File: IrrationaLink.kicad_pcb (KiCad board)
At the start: 2 copper layers, 50 x 24 mm, 27 parts, among them J1 USB_C_Receptacle_USB2.0, U1 ESP32-C3, U2 LM2937xMP

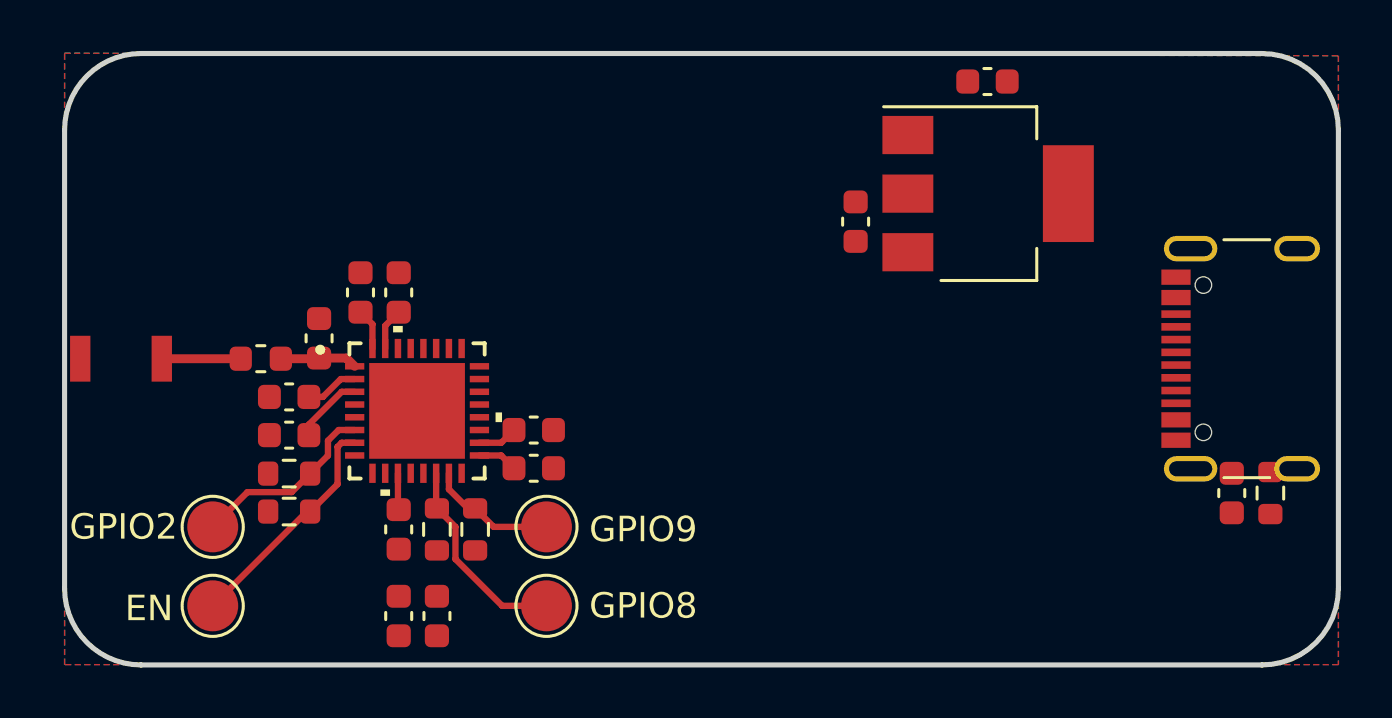
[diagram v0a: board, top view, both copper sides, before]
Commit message: Add gitignore; Route USB lines
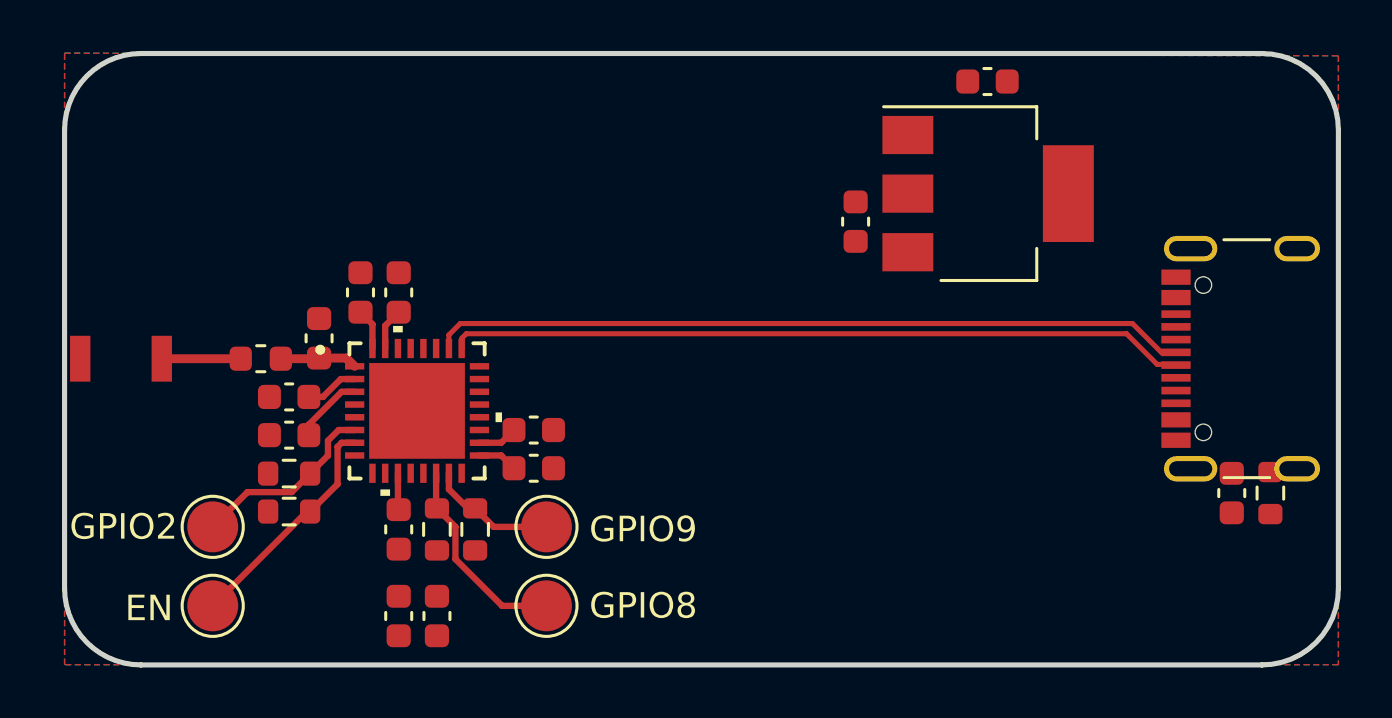
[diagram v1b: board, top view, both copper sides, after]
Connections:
- J1 pad A6: /D- -> /USB_D-
- J1 pad A7: /D+ -> /USB_D+
- J1 pad B6: /D- -> /USB_D-
- J1 pad B7: /D+ -> /USB_D+
- U1 pad 25: unconnected-(U1-GPIO18-Pad25) -> /USB_D-
- U1 pad 26: unconnected-(U1-GPIO19-Pad26) -> /USB_D+
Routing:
- net /USB_D+: track 0.00 -> 29.7 mm
- net /USB_D-: track 0.00 -> 29.0 mm

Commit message: Design first version of board (Crystal not routed yet)
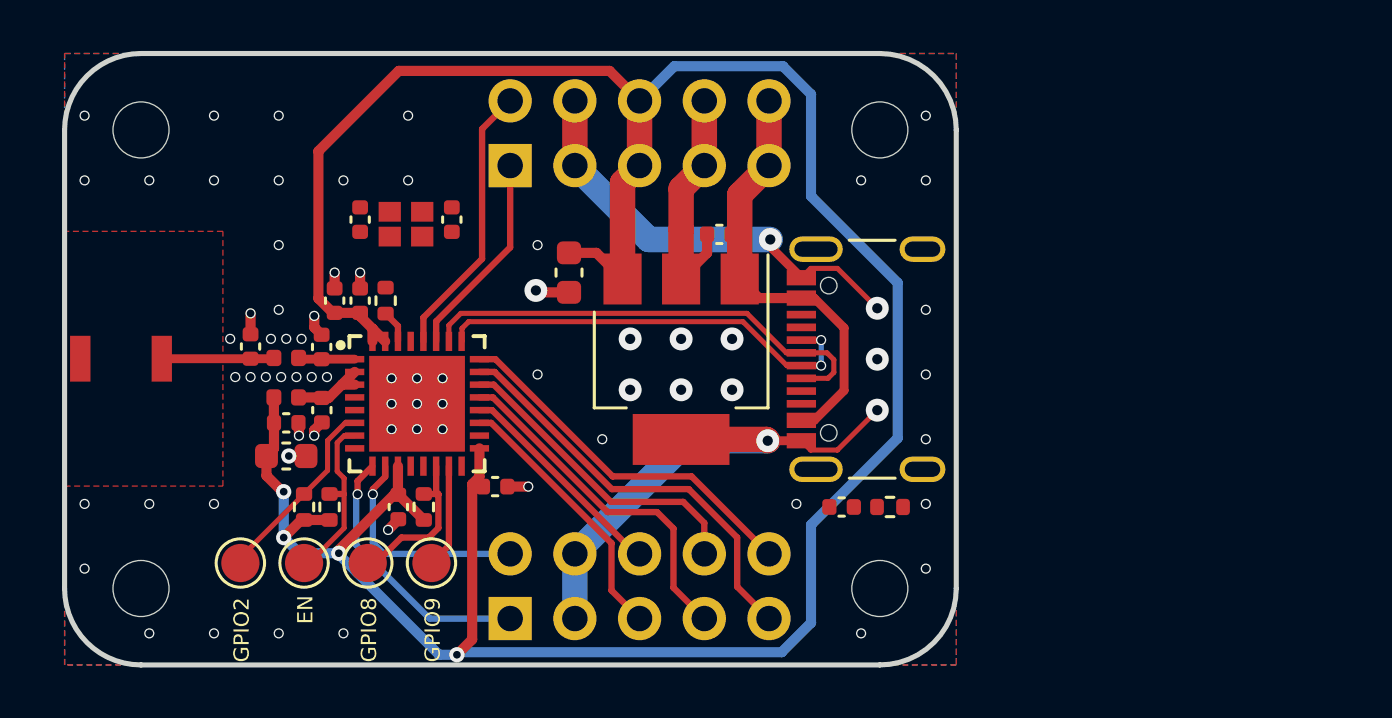
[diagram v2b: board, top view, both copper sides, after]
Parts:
- removed C10, C7: 100n, Capacitor_SMD:C_0603_1608Metric
- removed C8: 1u, Capacitor_SMD:C_0603_1608Metric
- removed C9: 4u7, Capacitor_SMD:C_0603_1608Metric
- removed R5: 10k, Resistor_SMD:R_0603_1608Metric
- added C14: C, Capacitor_SMD:C_0402_1005Metric, F.Cu at (126.3, 81.5)
- added C15: 100n, Capacitor_SMD:C_0402_1005Metric, F.Cu at (129.1, 84.0)
- added C16: 100n, Capacitor_SMD:C_0402_1005Metric, F.Cu at (127.7, 84.5)
- added C17: 100n, Capacitor_SMD:C_0402_1005Metric, F.Cu at (132.1, 87.8)
- added C18: 10u, Capacitor_SMD:C_0603_1608Metric, F.Cu at (127.7, 85.8)
- added H1: MountingHole, MountingHole:MountingHole_2.2mm_M2, F.Cu at (151.0, 91.0)
- added H2: MountingHole, MountingHole:MountingHole_2.2mm_M2, F.Cu at (151.0, 73.0)
- added H3: MountingHole, MountingHole:MountingHole_2.2mm_M2, F.Cu at (122.0, 73.0)
- added H4: MountingHole, MountingHole:MountingHole_2.2mm_M2, F.Cu at (122.0, 91.0)
- added J2: Conn_02x05_Odd_Even, Connector_PinHeader_2.54mm:PinHeader_2x05_P2.54mm_Vertical, F.Cu at (136.5, 92.2)
- added J3: Conn_02x05_Odd_Even, Connector_PinHeader_2.54mm:PinHeader_2x05_P2.54mm_Vertical, F.Cu at (136.5, 74.4)
- added L2: 2n, Inductor_SMD:L_0402_1005Metric, F.Cu at (127.7, 83.5)
- added R6: R, Resistor_SMD:R_0402_1005Metric, F.Cu at (131.6, 79.7)
- added Y1: ABM11W-32.0000MHZ-7-D1X-T3, encyclopedia_galactica:ABM11W-30.0000MHZ-7-D1X-T3, F.Cu at (132.4, 76.7)
- C1, C11, C2: footprint Capacitor_SMD:C_0603_1608Metric -> Capacitor_SMD:C_0402_1005Metric
- C12: value 1u -> 100n; footprint Capacitor_SMD:C_0603_1608Metric -> Capacitor_SMD:C_0402_1005Metric
- C13: value 1u -> 10u
- C3: value 100n -> 10n; footprint Capacitor_SMD:C_0603_1608Metric -> Capacitor_SMD:C_0402_1005Metric
- C4: value 100n -> 1u; footprint Capacitor_SMD:C_0603_1608Metric -> Capacitor_SMD:C_0402_1005Metric
- C5, C6: value 100n -> 12pF; footprint Capacitor_SMD:C_0603_1608Metric -> Capacitor_SMD:C_0402_1005Metric
- L1: footprint Inductor_SMD:L_0603_1608Metric -> Inductor_SMD:L_0402_1005Metric
- R1, R2, R3, R4: footprint Resistor_SMD:R_0603_1608Metric -> Resistor_SMD:R_0402_1005Metric
- TP1, TP2, TP3, TP4: footprint TestPoint:TestPoint_Pad_D2.0mm -> TestPoint:TestPoint_Pad_D1.5mm
- moved C11 15.3 mm to (149.5, 87.8), turned to 0 degrees
- moved R1 14.9 mm to (151.4, 87.8), turned to 180 degrees
- moved J1 14.7 mm to (151.6, 82.0)
- moved U2 13.7 mm to (143.2, 82.0), turned to -90 degrees
- moved C12 12.1 mm to (144.7, 77.1), turned to 180 degrees
- moved C13 11.4 mm to (138.8, 78.6), turned to -90 degrees
- moved C3 10.2 mm to (129.6, 79.7), turned to 90 degrees
- moved C4 9.11 mm to (130.6, 79.7), turned to 90 degrees
- moved C2 8.33 mm to (135.9, 87.0), turned to 0 degrees
- moved TP3 7.21 mm to (130.9, 90.0)
- moved TP2 4.73 mm to (133.4, 90.0)
- moved TP1 3.96 mm to (128.4, 90.0)
- moved C6 3.54 mm to (134.2, 76.5), turned to -90 degrees
- moved C5 2.86 mm to (130.6, 76.5)
- moved TP4 1.79 mm to (125.9, 90.0)
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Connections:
- C5 pad 1: +3V3 -> /XTAL_P
- C6 pad 1: +3V3 -> /XTAL_N
- U1 pad 10: unconnected-(U1-MTDI-Pad10) -> /ADC2_CH0
- U1 pad 18: +3V3 -> unconnected-(U1-VDD_SPI-Pad18)
- U1 pad 19: unconnected-(U1-SPIHD-Pad19) -> /GPIO12
- U1 pad 2: +3V3 -> /VDD3P3
- U1 pad 20: unconnected-(U1-SPIWP-Pad20) -> /GPIO13
- U1 pad 21: unconnected-(U1-SPICS0-Pad21) -> /GPIO14
- U1 pad 22: unconnected-(U1-SPICLK-Pad22) -> /GPIO15
- U1 pad 23: unconnected-(U1-SPID-Pad23) -> /GPIO16
- U1 pad 24: unconnected-(U1-SPIQ-Pad24) -> /GPIO17
- U1 pad 27: unconnected-(U1-U0RXD-Pad27) -> /U0RXD
- U1 pad 28: unconnected-(U1-U0TXD-Pad28) -> /U0TXD
- U1 pad 29: unconnected-(U1-XTAL_N-Pad29) -> /XTAL_N
- U1 pad 3: +3V3 -> /VDD3P3
- U1 pad 30: unconnected-(U1-XTAL_P-Pad30) -> /XTAL_P_RES
- U1 pad 9: unconnected-(U1-MTMS-Pad9) -> /ADC1_CH4
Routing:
- net +3V3: track 12.7 -> 110.7 mm, vias 0 -> 4
- net GND: track 0.00 -> 54.7 mm, vias 0 -> 74
- net VBUS: track 0.00 -> 17.0 mm
- net /GPIO16: track 0.00 -> 16.5 mm
- net /GPIO17: track 0.00 -> 14.5 mm
- net /GPIO14: track 0.00 -> 13.8 mm
- net /GPIO15: track 0.00 -> 12.3 mm
- net /USB_D-: track 29.0 -> 17.2 mm, vias 0 -> 2
- net /USB_D+: track 29.7 -> 18.6 mm
- net /U0TXD: track 0.00 -> 10.9 mm
- net /ADC1_CH4: track 0.00 -> 10.6 mm, vias 0 -> 1
- net /GPIO12: track 0.00 -> 10.6 mm
- net /ADC2_CH0: track 0.00 -> 8.78 mm, vias 0 -> 1
- net /GPIO13: track 0.00 -> 8.62 mm
- net /U0RXD: track 0.00 -> 8.10 mm
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- added copper zone on F.Cu, net GND
- removed copper zone on F.Cu, net unconnected-(U1-MTDO-Pad13)
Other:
- board size 50 x 24 mm -> 35 x 24 mm
- board text added: "+3V3"
- board text added: "12"
- board text added: "13"
- board text added: "14"
- board text added: "15"
- board text added: "16"
- board text added: "17"
- board text added: "ADC1_CH4"
- board text added: "ADC2_CH0"
- board text added: "EN"
- board text added: "GND"
- board text added: "GPIO2"
- board text added: "GPIO8"
- board text added: "GPIO9"
- board text added: "GPIOx"
- board text added: "IrrationaLink v1.0"
- board text added: "U0RXD"
- board text added: "U0TXD"
- board text added: "VBUS"

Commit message: Remove board name; Minor other changes
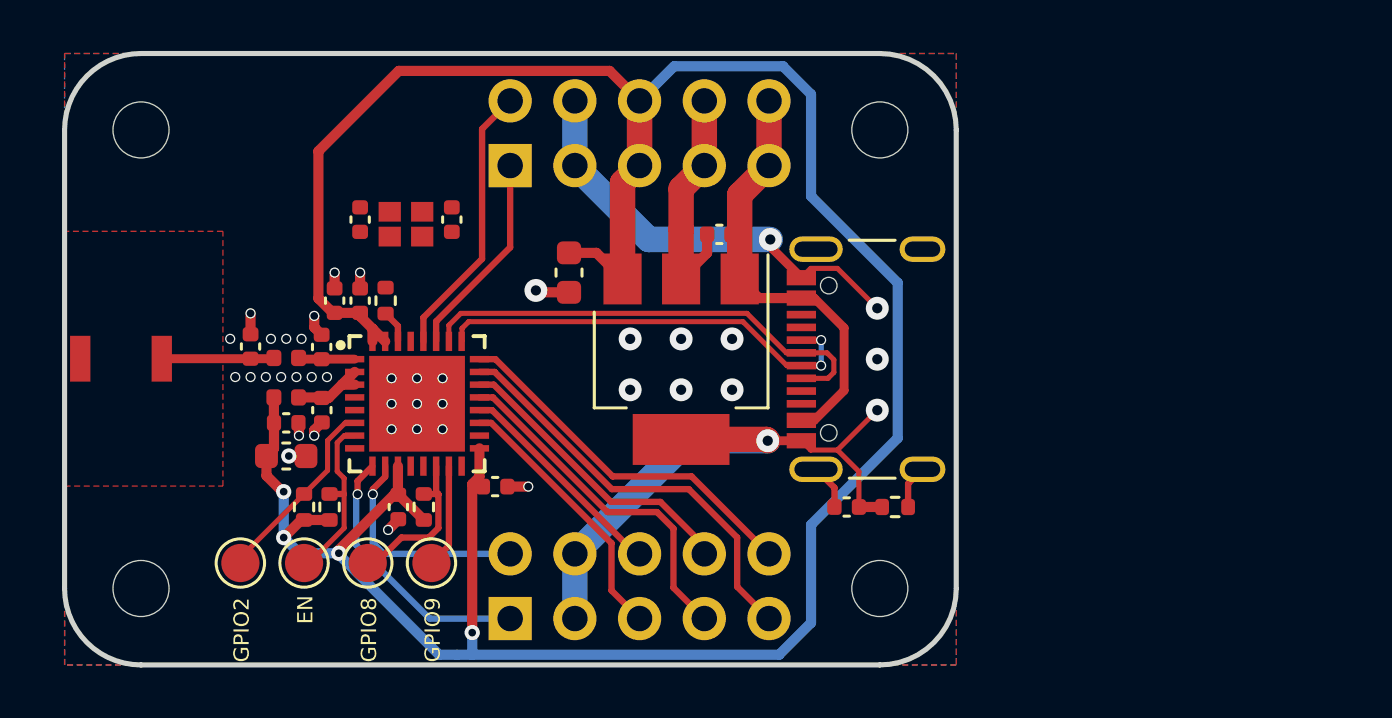
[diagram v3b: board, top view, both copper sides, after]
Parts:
- moved C11 0.20 mm to (149.7, 87.8)
- moved R1 0.20 mm to (151.6, 87.8)
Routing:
- net GND: track 54.7 -> 58.2 mm, vias 74 -> 41
- net /SHIELD: track 0.00 -> 3.49 mm
- net /GPIO15: track 12.3 -> 11.8 mm
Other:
- board text removed: "IrrationaLink v1.0"

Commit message: Add button; Move power lines
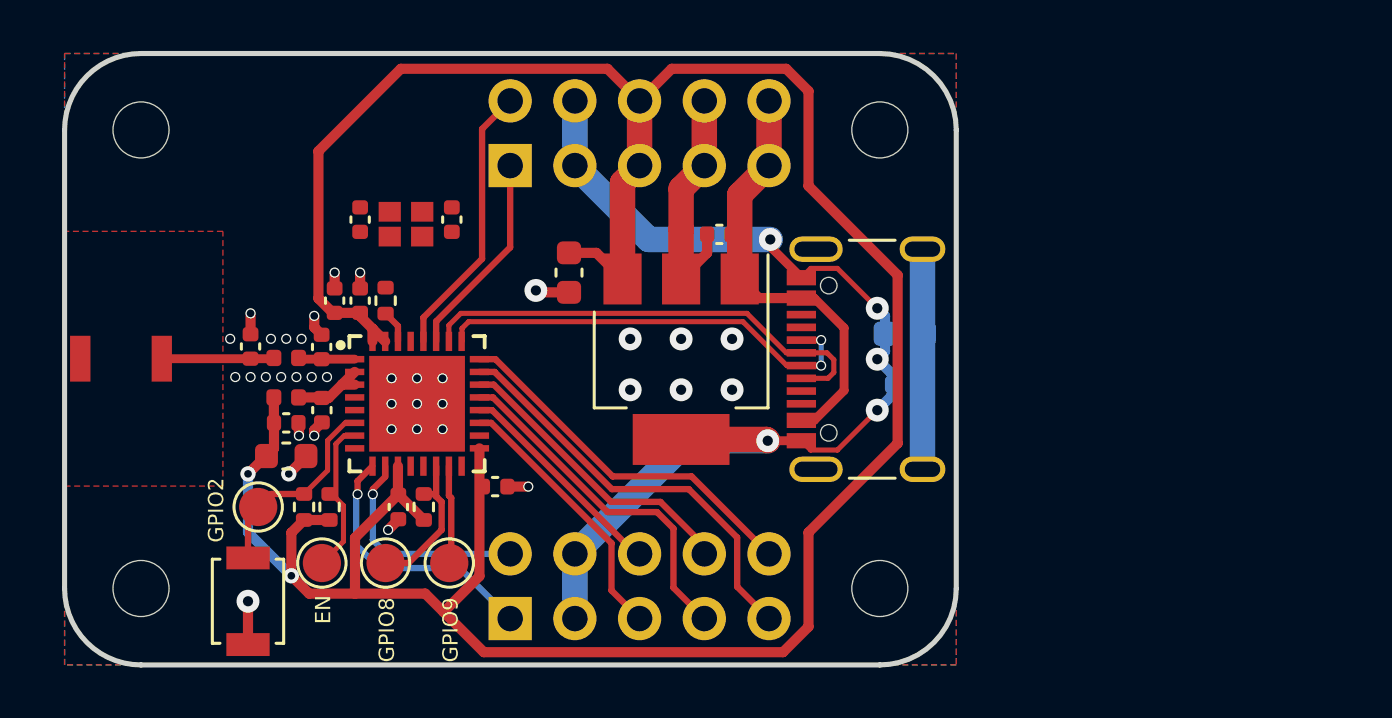
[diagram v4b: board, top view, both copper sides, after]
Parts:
- added SW1: SW_Push, Button_Switch_SMD:SW_SPST_B3U-1000P, F.Cu at (126.2, 91.5)
- C11: footprint Capacitor_SMD:C_0402_1005Metric -> Capacitor_SMD:C_0603_1608Metric; moved to B.Cu
- R1: moved to B.Cu
- moved C11 7.17 mm to (152.0, 81.0), turned to 180 degrees
- moved R1 4.82 mm to (152.0, 83.0)
- moved TP4 2.31 mm to (126.6, 87.8)
- moved TP1 0.70 mm to (129.1, 90.0)
- moved TP2 0.70 mm to (134.1, 90.0)
- moved TP3 0.70 mm to (131.6, 90.0)
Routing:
- net /SHIELD: track 3.49 -> 8.64 mm
- net GND: track 58.2 -> 61.4 mm, vias 41 -> 42
- net +3V3: track 110.5 -> 113.0 mm, vias 4 -> 2
- net /EN: track 6.98 -> 6.02 mm
- net /GPIO8: track 6.38 -> 5.85 mm

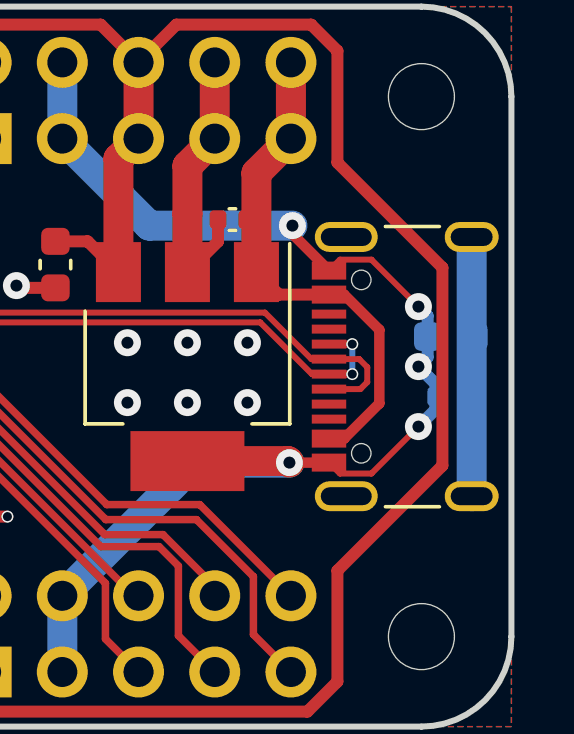
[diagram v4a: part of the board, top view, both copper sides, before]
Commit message: Move shield resistor and cap to front
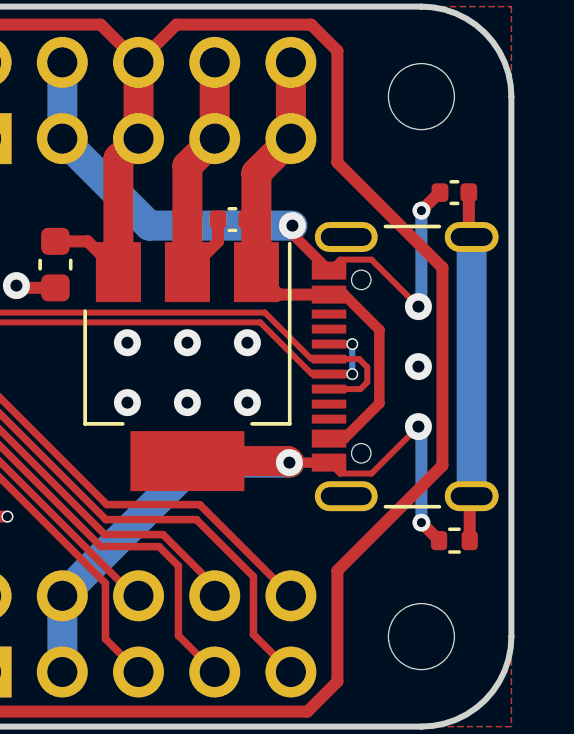
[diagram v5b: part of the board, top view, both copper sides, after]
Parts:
- C11: footprint Capacitor_SMD:C_0603_1608Metric -> Capacitor_SMD:C_0402_1005Metric; moved to F.Cu
- R1: moved to F.Cu
- moved C11 4.80 mm to (152.1, 76.2)
- moved R1 4.80 mm to (152.1, 87.8)
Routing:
- net GND: track 61.4 -> 64.9 mm, vias 42 -> 44
- net /SHIELD: track 8.64 -> 11.7 mm
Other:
- board text added: "HyperLink v1.0"

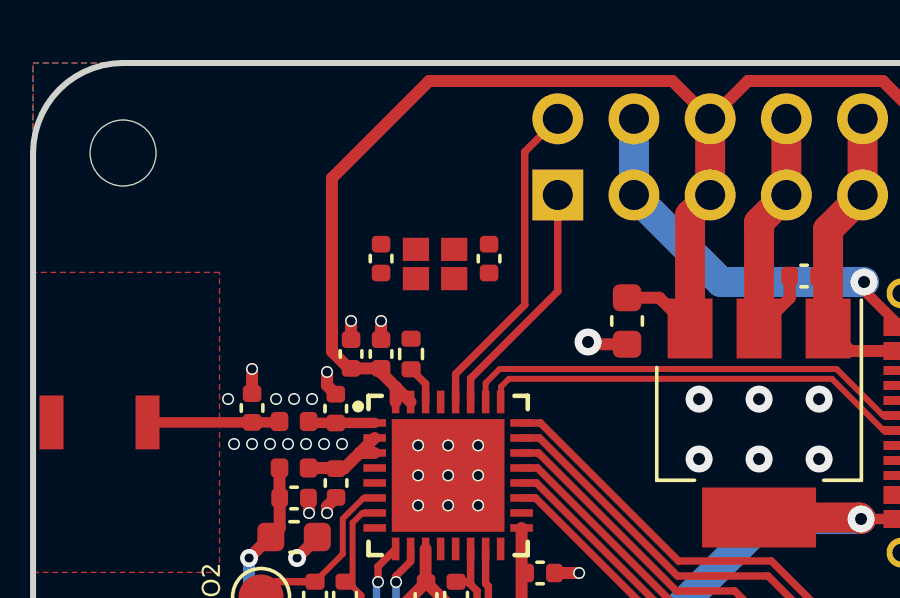
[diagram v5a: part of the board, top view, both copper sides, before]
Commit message: Connect Crystal; Add 500R resistor to U0TXD
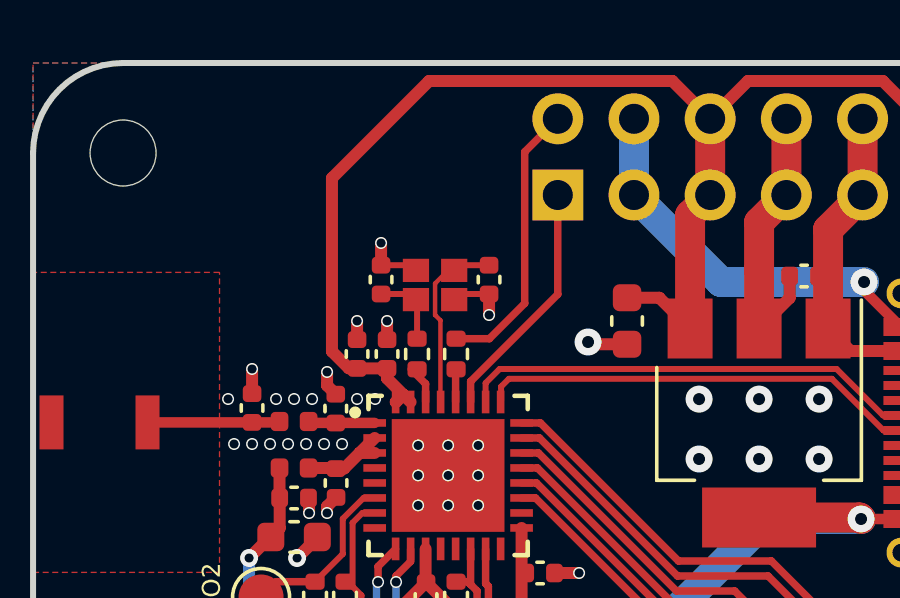
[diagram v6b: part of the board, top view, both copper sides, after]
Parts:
- added R5: 500R, Resistor_SMD:R_0402_1005Metric, F.Cu at (133.1, 79.7)
- R6: value R -> 0R
- Y1: value ABM11W-32.0000MHZ-7-D1X-T3 -> ABM11W-40.0000MHZ-8-B1U-T3
- moved C5 0.70 mm to (130.6, 77.2)
- moved C6 0.70 mm to (134.2, 77.2)
- moved Y1 0.70 mm to (132.4, 77.4)
- moved C3 0.20 mm to (129.8, 79.7)
- moved C4 0.20 mm to (130.8, 79.7)
- moved R6 0.20 mm to (131.8, 79.7)
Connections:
- U1 pad 28: /U0TXD -> /U0TXD_RES
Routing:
- net /XTAL_N: track 0.00 -> 6.08 mm
- net GND: track 64.9 -> 68.8 mm, vias 44 -> 48
- net /XTAL_P: track 0.00 -> 2.56 mm
- net /U0TXD: track 10.9 -> 9.38 mm
- net /U0TXD_RES: track 0.00 -> 0.93 mm
